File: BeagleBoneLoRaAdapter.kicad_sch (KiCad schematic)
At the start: 1 part, among them J3 Conn_02x23_Odd_Even

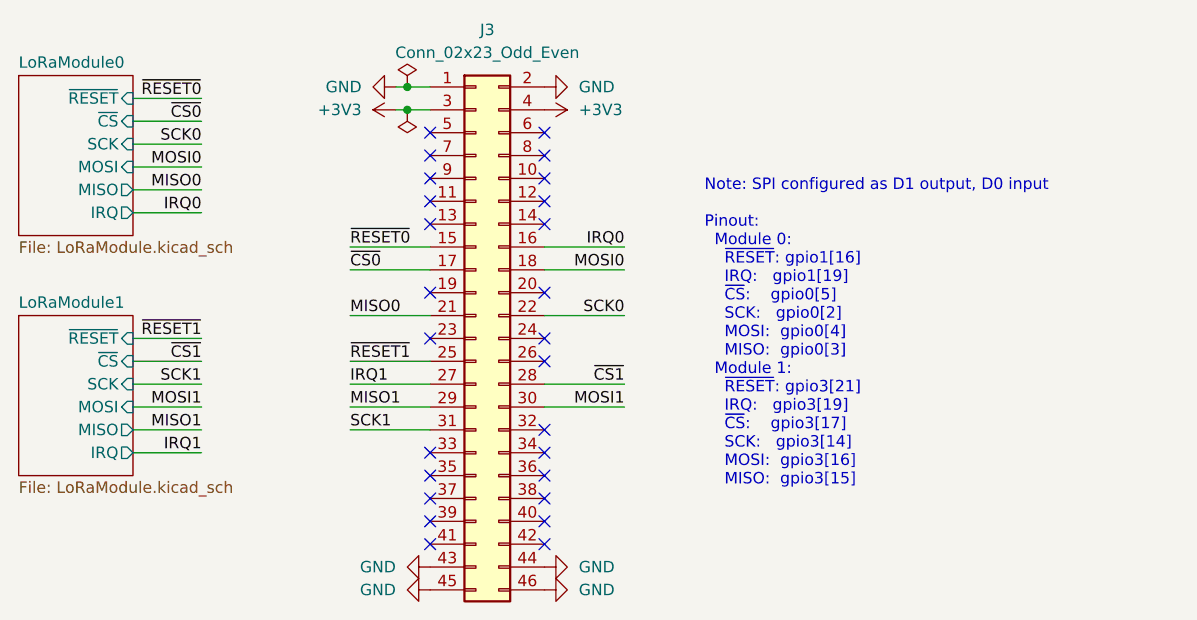
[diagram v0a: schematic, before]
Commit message: Add Px_y pin names on schematic
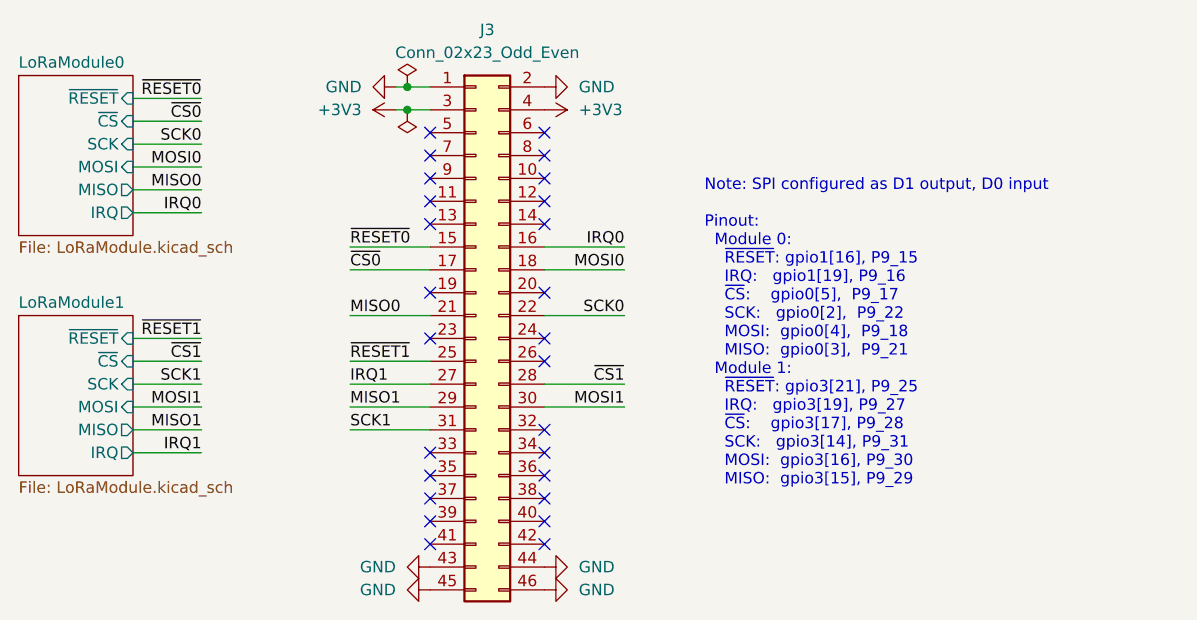
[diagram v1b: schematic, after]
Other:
- note added: "Note: SPI configured as D1 output, D0 input Pinout: Module 0: ~{RESET}: gpio1[16], P9_15 IRQ: gpio1[19], P9_16 ~{CS}: gpio0[5], P9_17 SCK: gpio0[2], P9_22 MOSI: gpio0[4], P9_18 MISO: gpio0[3], P9_21 Module 1: ~{RESET}: gpio3[21], P9_25 IRQ: gpio3[19], P9_27 ~{CS}: gpio3[17], P9_28 SCK: gpio3[14], P9_31 MOSI: gpio3[16], P9_30 MISO: gpio3[15], P9_29"
- note removed: "Note: SPI configured as D1 output, D0 input Pinout: Module 0: ~{RESET}: gpio1[16] IRQ: gpio1[19] ~{CS}: gpio0[5] SCK: gpio0[2] MOSI: gpio0[4] MISO: gpio0[3] Module 1: ~{RESET}: gpio3[21] IRQ: gpio3[19] ~{CS}: gpio3[17] SCK: gpio3[14] MOSI: gpio3[16] MISO: gpio3[15]"
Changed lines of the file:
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@@
     (stroke (width 0) (type default) (color 0 0 0 0))
   )
-  (text "Note: SPI configured as D1 output, D0 input\n\nPinout:\n  Module 0:\n    ~{RESET}: gpio1[16]\n    IRQ:   gpio1[19]\n    ~{CS}:    gpio0[5]\n    SCK:   gpio0[2]\n    MOSI:  gpio0[4]\n    MISO:  gpio0[3]\n  Module 1:\n    ~{RESET}: gpio3[21]\n    IRQ:   gpio3[19]\n    ~{CS}:    gpio3[17]\n    SCK:   gpio3[14]\n    MOSI:  gpio3[16]\n    MISO:  gpio3[15]"
+  (text "Note: SPI configured as D1 output, D0 input\n\nPinout:\n  Module 0:\n    ~{RESET}: gpio1[16], P9_15\n    IRQ:   gpio1[19], P9_16\n    ~{CS}:    gpio0[5],  P9_17\n    SCK:   gpio0[2],  P9_22\n    MOSI:  gpio0[4],  P9_18\n    MISO:  gpio0[3],  P9_21\n  Module 1:\n    ~{RESET}: gpio3[21], P9_25\n    IRQ:   gpio3[19], P9_27\n    ~{CS}:    gpio3[17], P9_28\n    SCK:   gpio3[14], P9_31\n    MOSI:  gpio3[16], P9_30\n    MISO:  gpio3[15], P9_29"
     (at 139.7 80.01 0)
     (effects (font (size 1.27 1.27)) (justify left bottom))

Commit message: Add BOM
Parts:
- J3: Manufacturer (none) -> Samtec; PartNumber (none) -> TSW-125-07-G-D
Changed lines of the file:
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@@
+      (effects (font (size 1.27 1.27)) hide)
+    )
+    (property "Manufacturer" "Samtec" (id 4) (at 114.3 63.5 0)
+      (effects (font (size 1.27 1.27)) hide)
+    )
+    (property "PartNumber" "TSW-125-07-G-D" (id 5) (at 114.3 63.5 0)
       (effects (font (size 1.27 1.27)) hide)
     )
